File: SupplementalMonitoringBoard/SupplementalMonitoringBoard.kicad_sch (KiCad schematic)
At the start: 1 part, among them U4 PAMC131M03QDFMRQ1

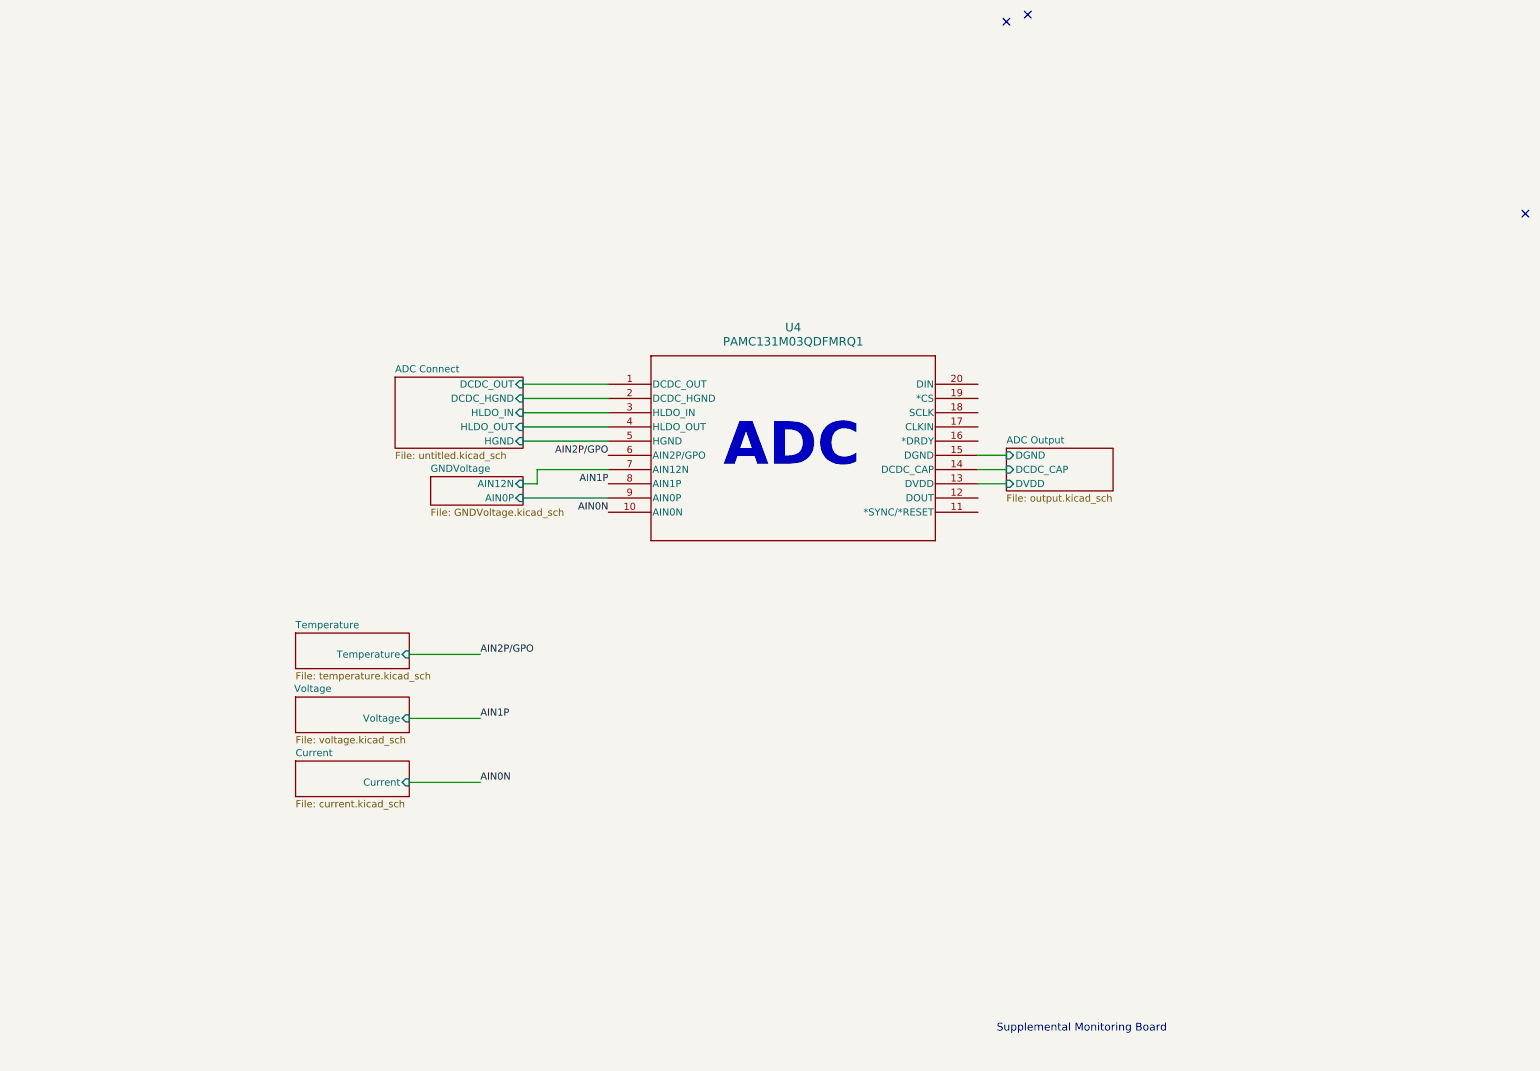
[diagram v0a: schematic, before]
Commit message: Supplemental Monitoring Board Changes
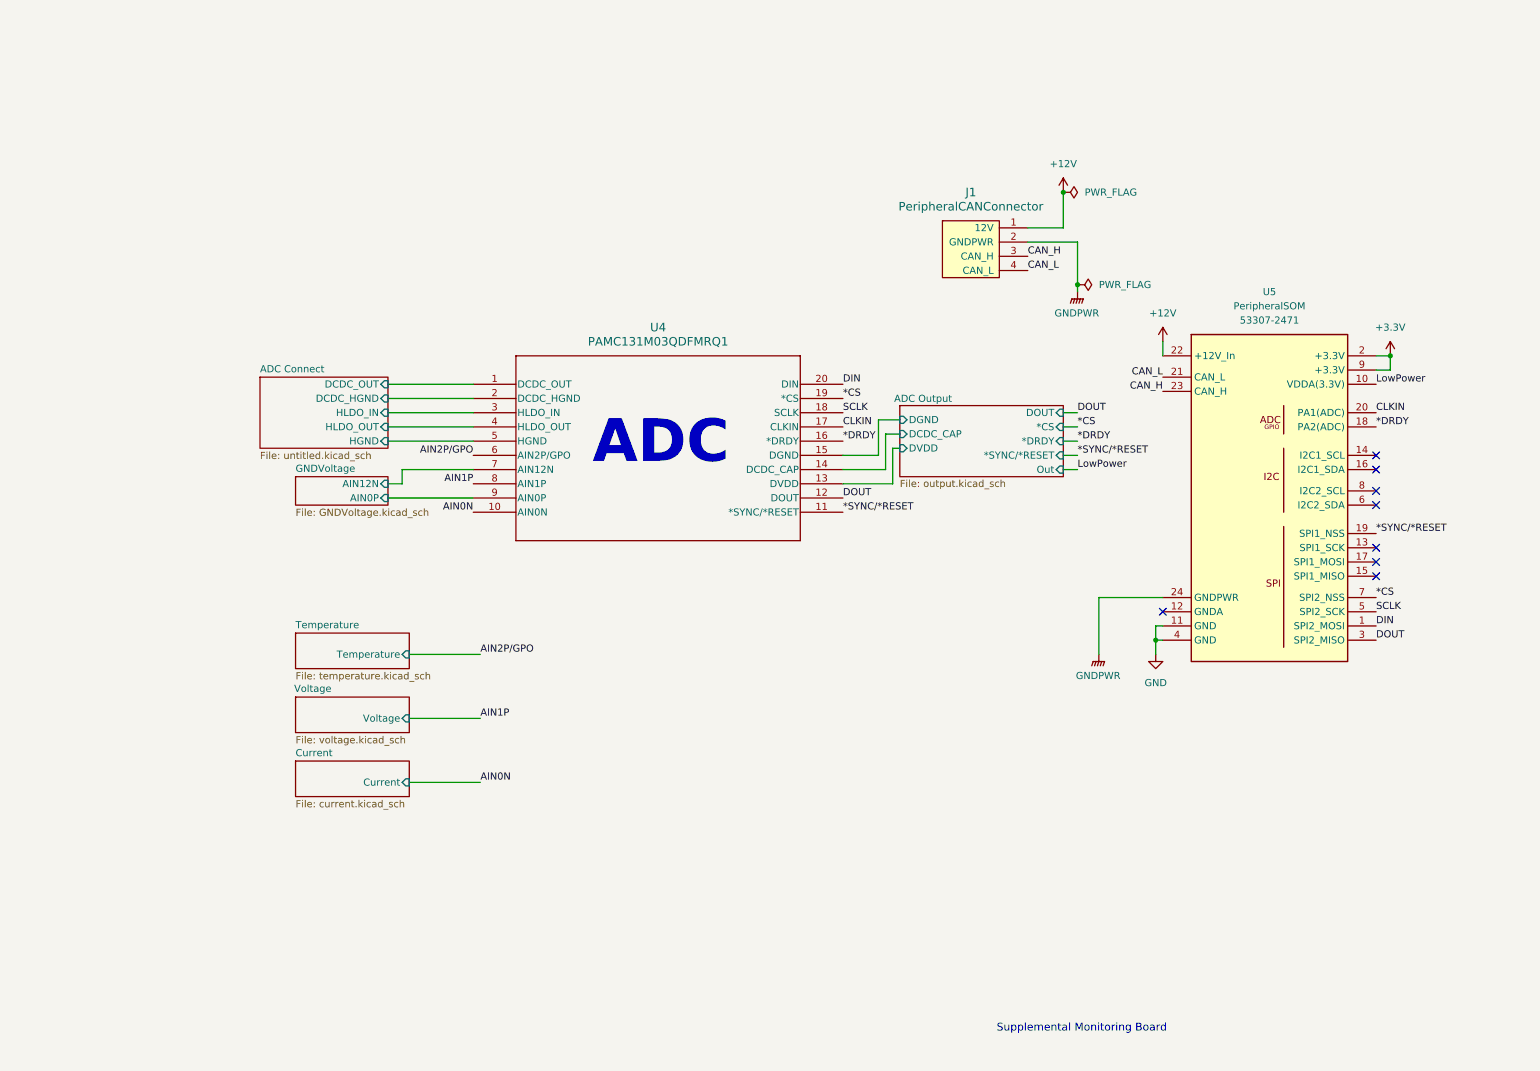
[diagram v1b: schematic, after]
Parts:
- added J1: PeripheralCANConnector, UTSVT_Connectors:Molex_MicroFit3.0_1x4xP3.00mm_PolarizingPeg_Vertical, symbol utsvt-connectors:PeripheralCANConnector
- added U5: PeripheralSOM, UTSVT_Special:PeripheralSOM, symbol utsvt-misc:PeripheralSOM
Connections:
- net *SYNC/*RESET: now reaches U4.11 (*SYNC/*RESET)
- net *SYNC/*RESET: now also U5.19 (SPI1_NSS)
- net DOUT: now reaches U4.12 (DOUT)
- net DOUT: now also U5.3 (SPI2_MISO)
- net *DRDY: now reaches U4.16 (*DRDY)
- net *DRDY: now also U5.18 (PA2(ADC))
- net CLKIN: now reaches U4.17 (CLKIN)
- net CLKIN: now also U5.20 (PA1(ADC))
- net SCLK: now reaches U4.18 (SCLK)
- net SCLK: now also U5.5 (SPI2_SCK)
- net *CS: now reaches U4.19 (*CS)
- net *CS: now also U5.7 (SPI2_NSS)
- net DIN: now reaches U4.20 (DIN)
- net DIN: now also U5.1 (SPI2_MOSI)
- new net +12V: J1.1 (12V), U5.22 (+12V_In)
- new net +3.3V: U5.2 (+3.3V), U5.9 (+3.3V)
- new net CAN_H: J1.3 (CAN_H), U5.23 (CAN_H)
- new net CAN_L: J1.4 (CAN_L), U5.21 (CAN_L)
- new net GND: U5.11 (GND), U5.4 (GND)
- new net GNDPWR: J1.2 (GNDPWR), U5.24 (GNDPWR)
- new net LowPower: U5.10 (VDDA(3.3V))
- no-connect marks 3 -> 8
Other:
- sheet ADC Output ports: added *CS, *DRDY, *SYNC/*RESET, DOUT, Out; removed none
- moved on the sheet: U4

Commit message: Supplemental Monitoring Board
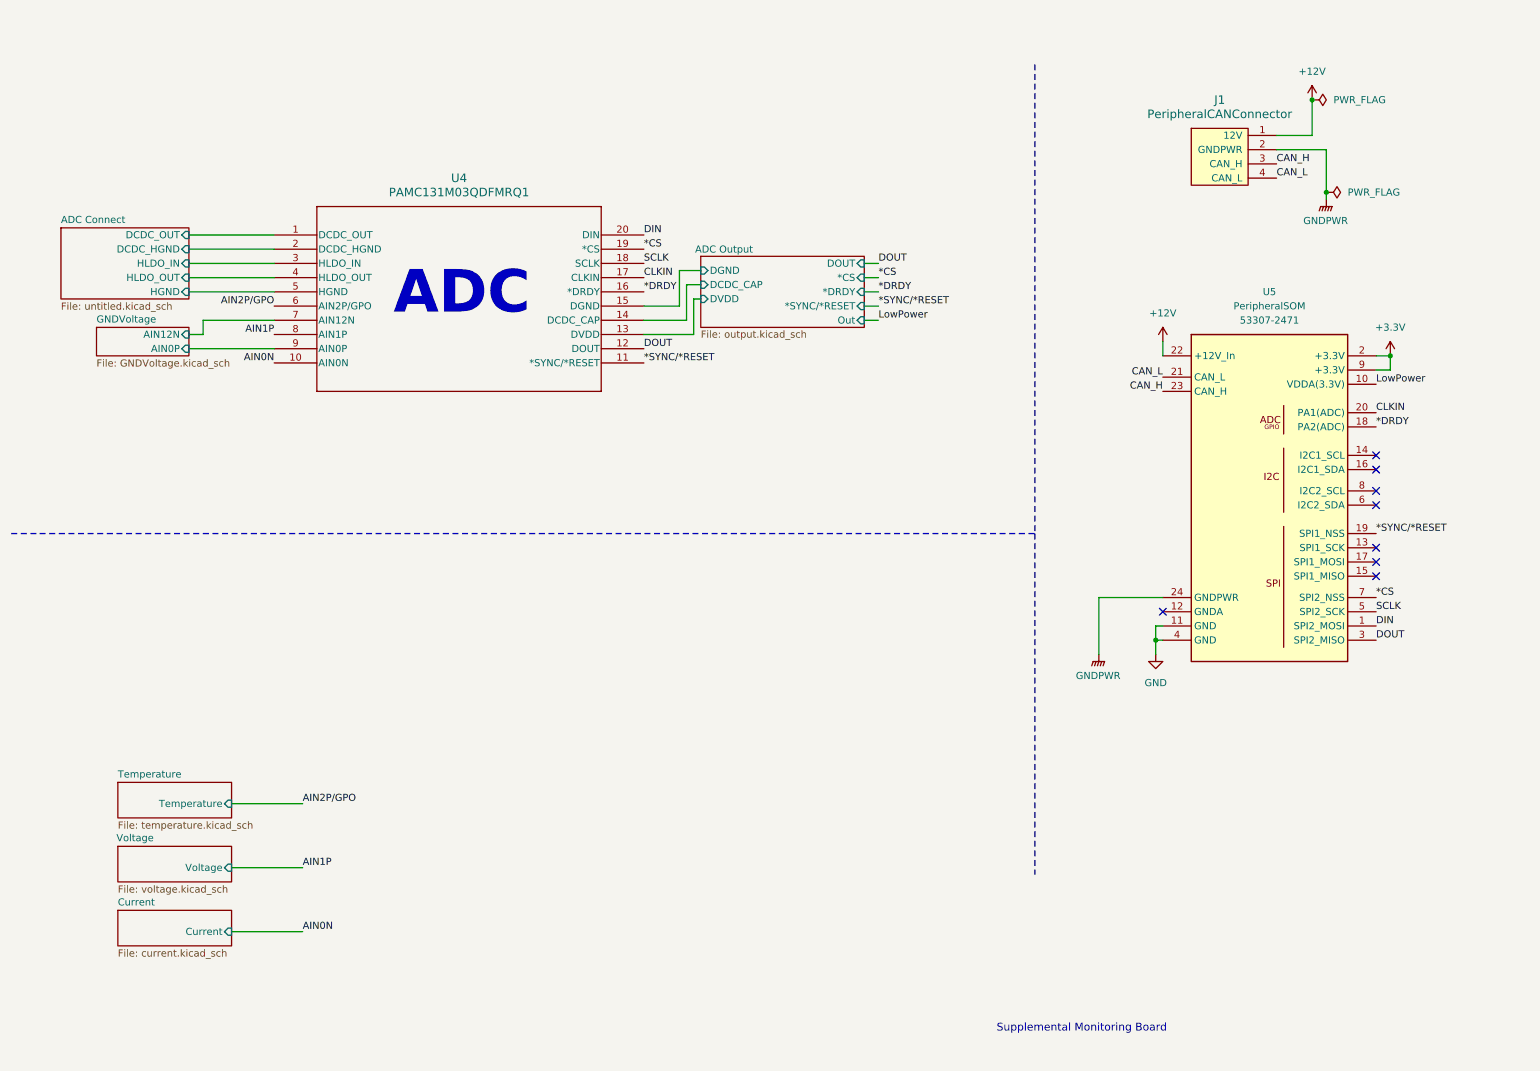
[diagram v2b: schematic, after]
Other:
- moved on the sheet: J1, U4

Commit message: Adressed Reviews - Supplemental Monitoring Board
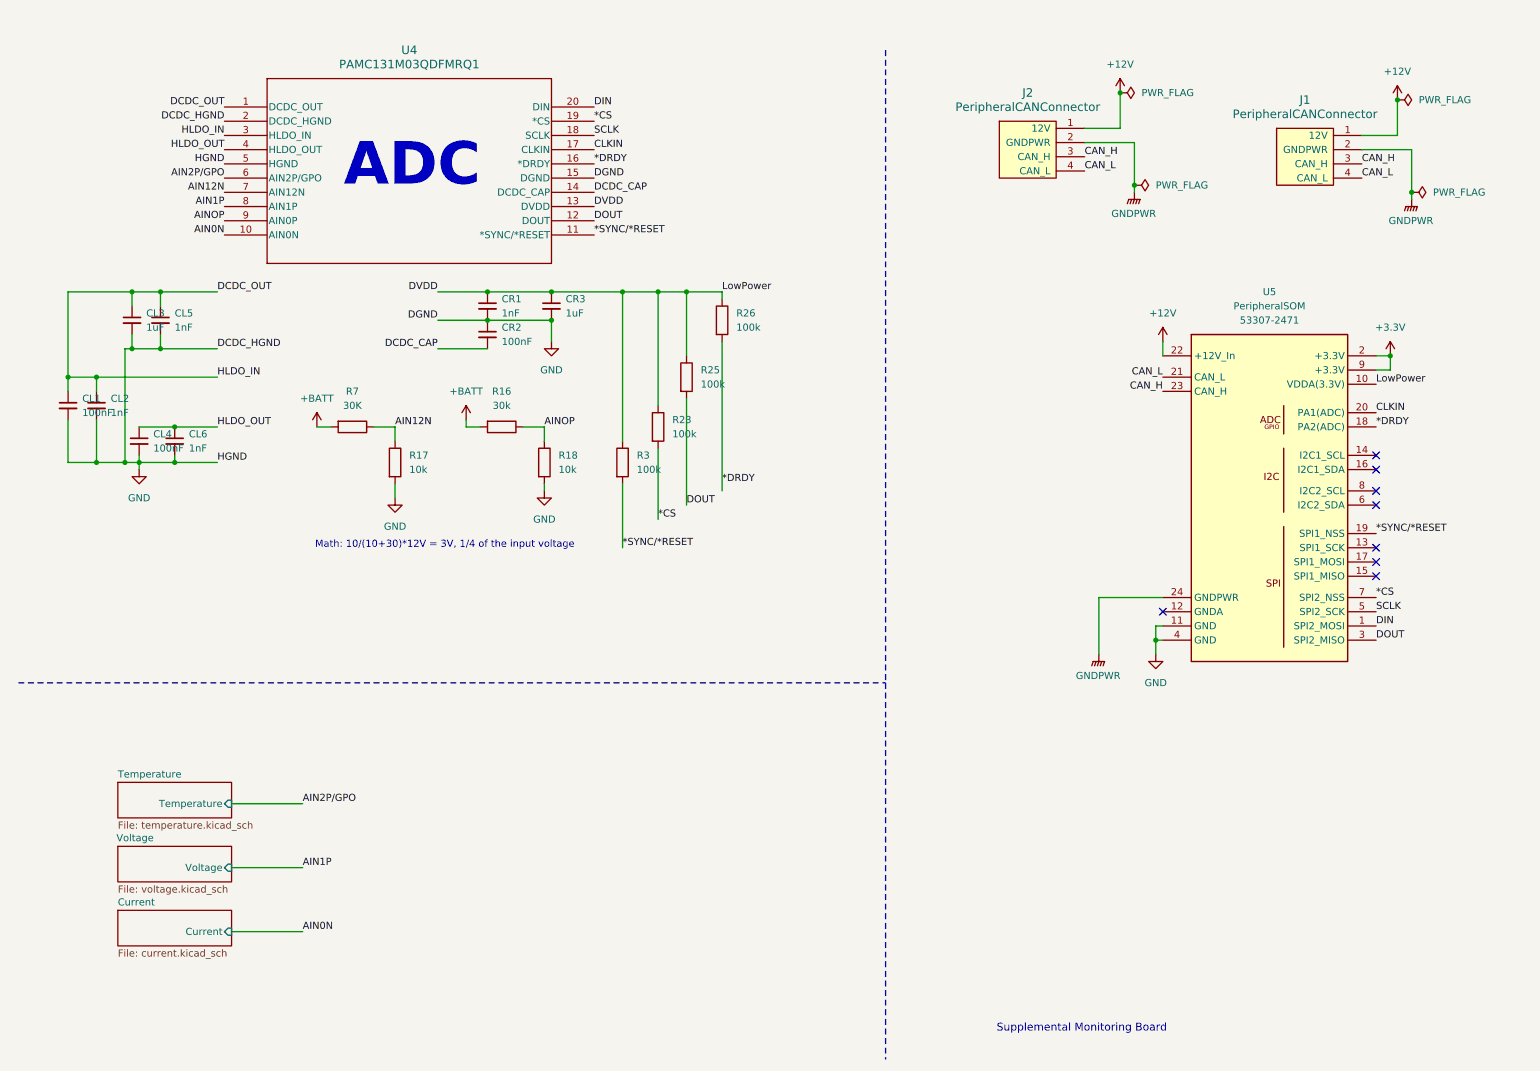
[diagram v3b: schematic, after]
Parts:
- added CL1, CL4, CR2: 100nF, Capacitor_SMD:C_0805_2012Metric, symbol Device:C_Small
- added CL2, CL5, CL6, CR1: 1nF, Capacitor_SMD:C_0805_2012Metric, symbol Device:C_Small
- added CL3, CR3: 1uF, Capacitor_SMD:C_0805_2012Metric, symbol Device:C_Small
- added J2: PeripheralCANConnector, UTSVT_Connectors:Molex_MicroFit3.0_1x4xP3.00mm_PolarizingPeg_Vertical, symbol utsvt-connectors:PeripheralCANConnector
- added R16: 30k, Resistor_SMD:R_0805_2012Metric, symbol Device:R
- added R17, R18: 10k, Resistor_SMD:R_0805_2012Metric, symbol Device:R
- added R23, R25, R26, R3: 100k, Resistor_SMD:R_0805_2012Metric, symbol Device:R
- added R7: 30K, Resistor_SMD:R_0805_2012Metric, symbol Device:R
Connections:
- net ADC Connect/DCDC_HGND is gone; now on net GND: U4.2 (DCDC_HGND)
- net ADC Connect/HGND is gone; now on net GND: U4.5 (HGND)
- net ADC Connect/HLDO_IN is gone; now on net DCDC_OUT: U4.3 (HLDO_IN)
- net ADC Output/DGND is gone; now on net GND: U4.15 (DGND)
- net LowPower is gone; now on net DVDD: U5.10 (VDDA(3.3V))
- net *CS: now also R23.2
- net *DRDY: now also R26.2
- net *SYNC/*RESET: now also R3.2
- net +12V: now also J2.1 (12V)
- net CAN_H: now also J2.3 (CAN_H)
- net CAN_L: now also J2.4 (CAN_L)
- net DOUT: now also R25.2
- net GND: now also CL1.2, CL2.2, CL3.2, CL4.2, CL5.2, CL6.2, CR1.2, CR2.1, CR3.2, R17.2, R18.2
- net GNDPWR: now also J2.2 (GNDPWR)
- net ADC Connect/DCDC_OUT renamed DCDC_OUT
- net DCDC_OUT: now also CL1.1, CL2.1, CL3.1, CL5.1
- net ADC Connect/HLDO_OUT renamed HLDO_OUT
- net HLDO_OUT: now also CL4.1, CL6.1
- net ADC Output/DCDC_CAP renamed DCDC_CAP
- net DCDC_CAP: now also CR2.2
- net ADC Output/DVDD renamed DVDD
- net DVDD: now also CR1.1, CR3.1, R23.1, R25.1, R26.1, R3.1
- net GNDVoltage/AIN0P renamed AINOP
- net AINOP: now also R16.1, R18.1
- net GNDVoltage/AIN12N renamed AIN12N
- net AIN12N: now also R17.1, R7.1
- new net +BATT: R16.2, R7.2
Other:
- removed sheet ADC Connect
- removed sheet ADC Output
- removed sheet GNDVoltage
- note added: "Math: 10/(10+30)*12V = 3V, 1/4 of the input voltage"
- moved on the sheet: J1, U4

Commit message: Supplemental MOnitoring Board
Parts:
- added J1: CarPowerConnector, Connector_Molex:Molex_Micro-Fit_3.0_43650-0215_1x02_P3.00mm_Vertical, symbol utsvt-connectors:CarPowerConnector
- added J2: CANconn, Connector_Molex:Molex_Micro-Fit_3.0_43650-0215_1x02_P3.00mm_Vertical, symbol Connector_Generic:Conn_01x02
- added J3: CANconn2, Connector_Molex:Molex_Micro-Fit_3.0_43650-0215_1x02_P3.00mm_Vertical, symbol Connector_Generic:Conn_01x02
- CL1, CL4, CR2: P/N (none) -> C0805C104M5RACTU
- CL2, CL5, CL6, CR1: value 1nF -> .1uF; P/N (none) -> C0805C102J5HACAUTO
- CL3, CR3: P/N (none) -> C0805C105K5PACTU
- J4: renamed from J2; now not fitted
- J5: renamed from J1; now not fitted
- R16: P/N (none) -> MCU08050D3002BP100
- R17, R18: P/N (none) -> CRCW080510K0FKEAC
- R23, R25, R26, R3: P/N (none) -> CRCW0805100KFKEAC
- R7: value 30K -> 30k; P/N (none) -> MCU08050D3002BP100
- U4: P/N (none) -> SBASAO3A
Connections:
- net +BATT is gone; now on net +12V: R16.2, R7.2
- net +12V: now also J1.1 (+12V)
- net +3.3V: no longer U5.9 (+3.3V)
- net CAN_H: now also J2.2 (Pin_2), J3.2 (Pin_2)
- net CAN_L: now also J2.1 (Pin_1), J3.1 (Pin_1)
- net DVDD: now also U5.9 (+3.3V); no longer U5.10 (VDDA(3.3V))
- net GND: now also J1.2 (GND)
- no-connect marks 8 -> 9

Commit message: Supplemental Monitoring Board
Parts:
- J1, J2, J3: P/N (none) -> 436500215
- R16, R7: P/N MCU08050D3002BP100 -> RCV0805330KFKEA
- R17, R18: P/N CRCW080510K0FKEAC -> RT0603FRE0710KL
- R23, R25, R26, R3: P/N CRCW0805100KFKEAC -> ERA-6VEB1003V
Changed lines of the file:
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@@
 			)
 		)
-		(property "Datasheet" ""
+		(property "Datasheet" "https://www.molex.com/molex/search/partSearch?query=436500215&pQuery="
 			(at 185.42 54.61 0)
 			(effects
@@
 			)
 		)
+		(property "P/N" "436500215"
+			(at 185.42 54.61 0)
+			(effects
+				(font
+					(size 1.27 1.27)
+				)
+				(hide yes)
+			)
+		)
 		(pin "1"
 		)
@@
 			)
 		)
-		(property "Datasheet" "https://www.vishay.com/docs/28700/mcx0x0xpre.pdf"
+		(property "Datasheet" "https://www.vishay.com/docs/20054/rcve3.pdf"
 			(at 73.66 82.55 0)
 			(effects
@@
 			)
 		)
-		(property "P/N" "MCU08050D3002BP100"
+		(property "P/N" "RCV0805330KFKEA"
 			(at 73.66 82.55 0)
 			(effects
@@
 			)
 		)
-		(property "Datasheet" "https://www.vishay.com/docs/28773/crcwce3.pdf"
+		(property "Datasheet" "https://www.mouser.com/catalog/specsheets/Panasonic_ERA.pdf"
 			(at 128.27 82.55 0)
 			(effects
@@
 			)
 		)
-		(property "P/N" "CRCW0805100KFKEAC"
+		(property "P/N" "ERA-6VEB1003V"
 			(at 128.27 82.55 0)
 			(effects
@@
 			)
 		)
-		(property "Datasheet" "~"
+		(property "Datasheet" "https://www.molex.com/molex/search/partSearch?query=436500215&pQuery="
 			(at 185.42 68.58 0)
 			(effects
@@
 			)
 		)
+		(property "P/N" "436500215"
+			(at 185.42 68.58 0)
+			(effects
+				(font
+					(size 1.27 1.27)
+				)
+				(hide yes)
+			)
+		)
 		(pin "2"
 		)
@@
 			)
 		)
-		(property "Datasheet" "https://www.mouser.com/datasheet/2/447/PYu_RT_1_to_0_01_RoHS_L_15-3461507.pdf"
+		(property "Datasheet" "https://www.mouser.com/ProductDetail/603-RT0603FRE0710KL"
 			(at 81.28 88.9 0)
 			(effects
@@
 			)
 		)
-		(property "P/N" "CRCW080510K0FKEAC"
+		(property "P/N" "RT0603FRE0710KL "
 			(at 81.28 88.9 0)
 			(effects
@@
 			)
 		)
-		(property "Datasheet" "https://www.vishay.com/docs/28700/mcx0x0xpre.pdf"
+		(property "Datasheet" "https://www.vishay.com/docs/20054/rcve3.pdf"
 			(at 100.33 82.55 0)
 			(effects
@@
 			)
 		)
-		(property "P/N" "MCU08050D3002BP100"
+		(property "P/N" "RCV0805330KFKEA"
 			(at 100.33 82.55 0)
 			(effects
@@
 			)
 		)
-		(property "Datasheet" "https://www.vishay.com/docs/28773/crcwce3.pdf"
+		(property "Datasheet" "https://www.mouser.com/catalog/specsheets/Panasonic_ERA.pdf"
 			(at 139.7 63.5 0)
 			(effects
@@
 			)
 		)
-		(property "P/N" "CRCW0805100KFKEAC"
+		(property "P/N" "ERA-6VEB1003V"
 			(at 139.7 63.5 0)
 			(effects
@@
 			)
 		)
-		(property "Datasheet" "https://www.vishay.com/docs/28773/crcwce3.pdf"
+		(property "Datasheet" "https://www.mouser.com/catalog/specsheets/Panasonic_ERA.pdf"
 			(at 121.92 88.9 0)
 			(effects
@@
 			)
 		)
-		(property "P/N" "CRCW0805100KFKEAC"
+		(property "P/N" "ERA-6VEB1003V"
 			(at 121.92 88.9 0)
 			(effects
@@
 			)
 		)
-		(property "Datasheet" "~"
+		(property "Datasheet" "https://www.molex.com/molex/search/partSearch?query=436500215&pQuery="
 			(at 185.42 76.2 0)
 			(effects
@@
 			)
 		)
+		(property "P/N" "436500215"
+			(at 185.42 76.2 0)
+			(effects
+				(font
+					(size 1.27 1.27)
+				)
+				(hide yes)
+			)
+		)
 		(pin "2"
 		)
@@
 			)
 		)
-		(property "Datasheet" "https://www.mouser.com/datasheet/2/447/PYu_RT_1_to_0_01_RoHS_L_15-3461507.pdf"
+		(property "Datasheet" "https://www.mouser.com/ProductDetail/603-RT0603FRE0710KL"
 			(at 107.95 88.9 0)
 			(effects
@@
 			)
 		)
-		(property "P/N" "CRCW080510K0FKEAC"
+		(property "P/N" "RT0603FRE0710KL "
 			(at 107.95 88.9 0)
 			(effects
@@
 			)
 		)
-		(property "Datasheet" "https://www.vishay.com/docs/28773/crcwce3.pdf"
+		(property "Datasheet" "https://www.mouser.com/catalog/specsheets/Panasonic_ERA.pdf"
 			(at 133.35 73.66 0)
 			(effects
@@
 			)
 		)
-		(property "P/N" "CRCW0805100KFKEAC"
+		(property "P/N" "ERA-6VEB1003V"
 			(at 133.35 73.66 0)
 			(effects
